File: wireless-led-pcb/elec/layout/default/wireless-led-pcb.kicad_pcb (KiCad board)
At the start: 2 copper layers, 40 x 40 mm, 37 parts

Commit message: Layout "done" but tbh it's super unverified.
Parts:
- added REF**: MountingHole_3.2mm_M3, MountingHole:MountingHole_3.2mm_M3, F.Cu at (49.0, 96.0)
- added REF**: MountingHole_3.2mm_M3, MountingHole:MountingHole_3.2mm_M3, F.Cu at (160.0, 85.0)
- added REF**: MountingHole_3.2mm_M3, MountingHole:MountingHole_3.2mm_M3, F.Cu at (180.0, 85.0)
- R4: value 100mW Thick Film Resistors 75V ±100ppm/℃ ±1% 732kΩ 0603 Chip Resistor - Surface Mount ROHS -> 100mW Thick Film Resistors 150V ±100ppm/℃ ±1% 732kΩ 0603 Chip Resistor - Surface Mount ROHS
- U10, U7, U8, U9: footprint TerminalBlock_Phoenix:TerminalBlock_Phoenix_MKDS-1,5-2_1x02_P5.00mm_Horizontal -> TerminalBlock_Phoenix:TerminalBlock_Phoenix_MKDS-1,5-3_1x03_P5.00mm_Horizontal
- moved U11 148.8 mm to (45.6, 79.4)
- moved U6 123.2 mm to (44.0, 91.0), turned to -90 degrees
- moved U8 74.0 mm to (171.0, 95.0), turned to 0 degrees
- moved U7 70.7 mm to (154.0, 95.0), turned to 0 degrees
- moved R2 62.8 mm to (115.5, 79.0), turned to 180 degrees
- moved U1 62.5 mm to (118.0, 75.0), turned to 180 degrees
- moved R1 56.4 mm to (120.5, 79.0)
- moved U9 55.1 mm to (181.0, 75.0), turned to 180 degrees
- moved Q1 51.5 mm to (90.5, 76.0), turned to 180 degrees
- moved R8 51.0 mm to (90.8, 79.0), turned to 180 degrees
- moved U4 46.4 mm to (107.2, 76.6), turned to 90 degrees
- moved C10 40.9 mm to (99.5, 73.0), turned to 180 degrees
- moved U15 40.5 mm to (125.3, 93.9), turned to -90 degrees
- moved U10 40.2 mm to (164.0, 75.0), turned to 180 degrees
- moved C7 38.5 mm to (83.5, 77.5), turned to 90 degrees
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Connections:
- C10 pad 1: ldo_5v-vcc -> level_shifter.ic-vcc
- Q1 pad 1: (no net) -> detect
- Q1 pad 2: (no net) -> boost_3v7_to_5v-vcc
- Q1 pad 3: (no net) -> led_strip_connector_1-vcc
- R8 pad 1: boost_3v7_to_5v-vcc -> detect
- U11 pad 1: (no net) -> led_strip_connector_1-vcc
- U11 pad 2: (no net) -> barrel_jack-vcc
- U11 pad 4: (no net) -> pole2_b
- U11 pad 5: (no net) -> battery_connector-vcc
- U14 pad 2: ldo_5v-vcc -> level_shifter.ic-vcc
- U4 pad 1: oe1 -> usb_connetor-gnd
- U4 pad 10: oe1 -> usb_connetor-gnd
- U4 pad 13: oe1 -> usb_connetor-gnd
- U4 pad 4: oe1 -> usb_connetor-gnd
- U4 pad 7: level_shifter.ic-gnd -> usb_connetor-gnd
- U5 pad 1: (no net) -> battery_connector-vcc
- U5 pad 2: (no net) -> usb_connetor-gnd
- U6 pad 1: (no net) -> barrel_jack-vcc
- U6 pad 2: (no net) -> usb_connetor-gnd
- U6 pad 3: (no net) -> detect
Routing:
- net led_strip_connector_1-vcc: track 0.00 -> 191.1 mm, vias 0 -> 3
- net battery_connector-vcc: track 0.00 -> 94.4 mm
- net mcu.ic-vcc-1: track 0.00 -> 90.6 mm, vias 0 -> 4
- net out2: track 0.00 -> 89.6 mm
- net out1: track 0.00 -> 74.2 mm
- net out3: track 0.00 -> 69.4 mm
- net usb_connetor-gnd: track 0.00 -> 61.6 mm, vias 0 -> 29
- net detect: track 0.00 -> 61.0 mm
- net boost_3v7_to_5v-vcc: track 0.00 -> 56.2 mm, vias 0 -> 2
- net out4: track 0.00 -> 55.2 mm
- net io14: track 0.00 -> 50.9 mm
- net pole2_b: track 0.00 -> 44.2 mm, vias 0 -> 1
- net io15: track 0.00 -> 42.8 mm
- net dp: track 0.00 -> 37.6 mm
- net dm: track 0.00 -> 37.0 mm
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- added copper zone on In1.Cu, net usb_connetor-gnd
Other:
- board size 40 x 40 mm -> 154 x 30 mm
- copper layers 2 -> 4

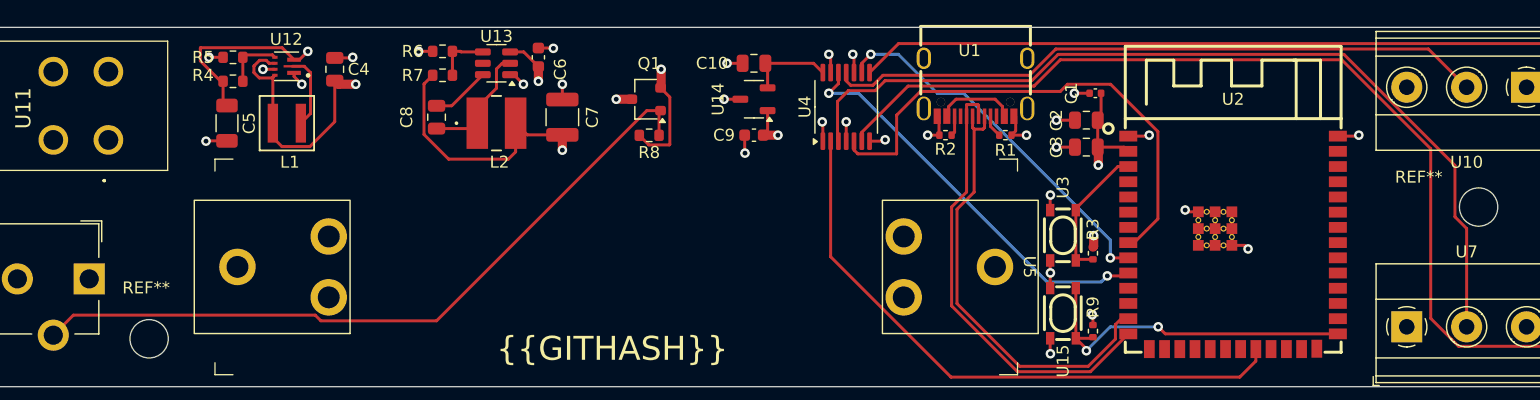
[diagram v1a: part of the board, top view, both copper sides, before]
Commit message: basic layout complete, smoke tested with jlcpcb.
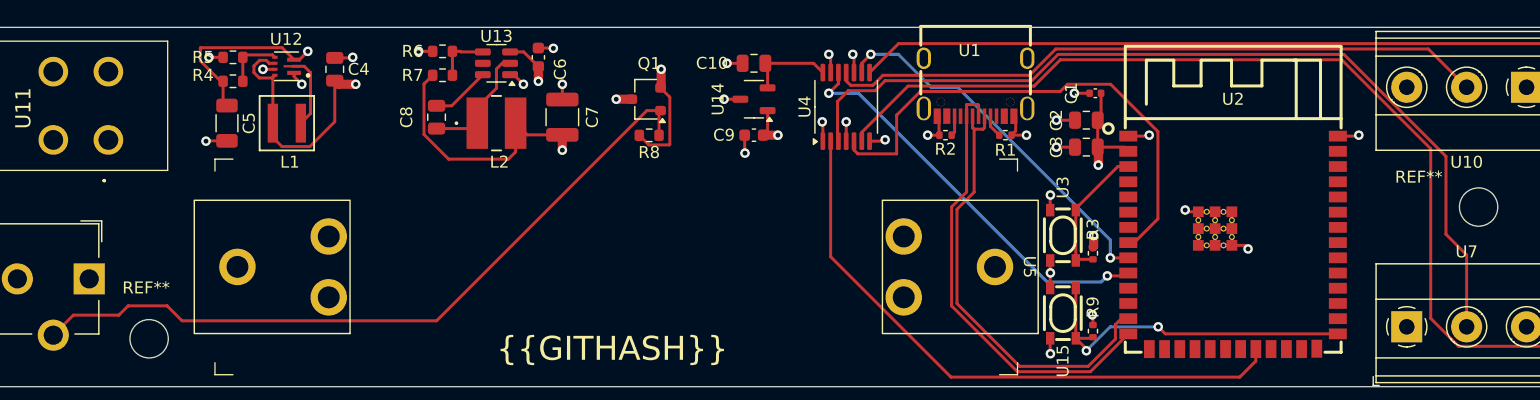
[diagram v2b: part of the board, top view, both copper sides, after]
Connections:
- U2 pad : (no net) -> usb_connetor-gnd
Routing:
- net usb_connetor-vcc: track 6.61 -> 0.00 mm
- net detect: track 61.0 -> 61.6 mm
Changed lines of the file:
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@@
 			(layers "*.Cu" "*.Paste" "*.Mask")
 			(remove_unused_layers no)
+			(net 8 "usb_connetor-gnd")
 		)
 		(pad "" thru_hole circle
@@
 			(layers "*.Cu" "*.Paste" "*.Mask")
 			(remove_unused_layers no)
+			(net 8 "usb_connetor-gnd")
 		)
 		(pad "" thru_hole circle
@@
 			(layers "*.Cu" "*.Paste" "*.Mask")
 			(remove_unused_layers no)
+			(net 8 "usb_connetor-gnd")
 		)
 		(pad "" thru_hole circle
@@
 			(layers "*.Cu" "*.Paste" "*.Mask")
 			(remove_unused_layers no)
+			(net 8 "usb_connetor-gnd")
 		)
 		(pad "" thru_hole circle
@@
 			(layers "*.Cu" "*.Paste" "*.Mask")
 			(remove_unused_layers no)
+			(net 8 "usb_connetor-gnd")
 		)
 		(pad "" thru_hole circle
@@
 			(layers "*.Cu" "*.Paste" "*.Mask")
 			(remove_unused_layers no)
+			(net 8 "usb_connetor-gnd")
 		)
 		(pad "" thru_hole circle
@@
 			(layers "*.Cu" "*.Paste" "*.Mask")
 			(remove_unused_layers no)
+			(net 8 "usb_connetor-gnd")
 		)
 		(pad "" thru_hole circle
@@
 			(layers "*.Cu" "*.Paste" "*.Mask")
 			(remove_unused_layers no)
+			(net 8 "usb_connetor-gnd")
 		)
 		(pad "" thru_hole circle
@@
 			(layers "*.Cu" "*.Paste" "*.Mask")
 			(remove_unused_layers no)
+			(net 8 "usb_connetor-gnd")
 		)
 		(pad "" thru_hole circle
@@
 			(layers "*.Cu" "*.Paste" "*.Mask")
 			(remove_unused_layers no)
+			(net 8 "usb_connetor-gnd")
 		)
 		(pad "" thru_hole circle
@@
 			(layers "*.Cu" "*.Paste" "*.Mask")
 			(remove_unused_layers no)
+			(net 8 "usb_connetor-gnd")
 		)
 		(pad "" thru_hole circle
@@
 			(layers "*.Cu" "*.Paste" "*.Mask")
 			(remove_unused_layers no)
+			(net 8 "usb_connetor-gnd")
 		)
 		(pad "1" smd rect
@@
 	)
 	(segment
-		(start 129.25 87.75)
-		(end 129.25 89.25)
+		(start 114.304695 75)
+		(end 116.5 75)
 		(width 0.25)
 		(layer "B.Cu")
@@
 	)
 	(segment
-		(start 114.809695 75.505)
-		(end 117.005 75.505)
+		(start 116.5 75)
+		(end 129.25 87.75)
 		(width 0.25)
 		(layer "B.Cu")
@@
 	)
 	(segment
-		(start 111.554695 72.25)
-		(end 114.809695 75.505)
+		(start 129.25 87.75)
+		(end 129.25 89.25)
 		(width 0.25)
 		(layer "B.Cu")
@@
 	)
 	(segment
-		(start 117.005 75.505)
-		(end 129.25 87.75)
+		(start 109.25 72.25)
+		(end 111.554695 72.25)
 		(width 0.25)
 		(layer "B.Cu")
@@
 	)
 	(segment
-		(start 109.25 72.25)
-		(end 111.554695 72.25)
+		(start 111.554695 72.25)
+		(end 114.304695 75)
 		(width 0.25)
 		(layer "B.Cu")
@@
 	)
 	(segment
-		(start 115.75 76.615305)
-		(end 115.75 77.41)
-		(width 0.25)
-		(layer "F.Cu")
-		(net 40)
-	)
-	(segment
-		(start 116.370305 75.995)
-		(end 115.75 76.615305)
-		(width 0.25)
-		(layer "F.Cu")
-		(net 40)
-	)
-	(segment
-		(start 120.25 77.42)
-		(end 120.25 76.615305)
-		(width 0.25)
-		(layer "F.Cu")
-		(net 40)
-	)
-	(segment
-		(start 120.25 76.615305)
-		(end 119.629695 75.995)
-		(width 0.25)
-		(layer "F.Cu")
-		(net 40)
-	)
-	(segment
-		(start 119.629695 75.995)
-		(end 116.370305 75.995)
-		(width 0.25)
-		(layer "F.Cu")
-		(net 40)
-	)
-	(segment
 		(start 116.25 78.75)
 		(end 116 79)
@@
 	)
 	(segment
-		(start 148.755 72.255)
-		(end 124.889544 72.255)
+		(start 107.384792 75.2875)
+		(end 107.380048 75.282757)
 		(width 0.25)
 		(layer "F.Cu")
@@
 	)
 	(segment
-		(start 124.889544 72.255)
-		(end 122.694544 74.45)
+		(start 159 89)
+		(end 157.274102 87.274102)
 		(width 0.25)
 		(layer "F.Cu")
@@
 	)
 	(segment
-		(start 107.380048 75.282757)
-		(end 106.475 76.187805)
+		(start 106.475 79.425)
+		(end 106.55 79.5)
 		(width 0.25)
 		(layer "F.Cu")
@@
 	)
 	(segment
-		(start 158.025 85.818072)
-		(end 158.025 81.525)
+		(start 157.274102 87.274102)
+		(end 157.274102 80.774102)
 		(width 0.25)
 		(layer "F.Cu")
@@
 	)
 	(segment
-		(start 110.452708 74.45)
-		(end 109.615208 75.2875)
+		(start 124.889544 72.255)
+		(end 122.694544 74.45)
 		(width 0.25)
 		(layer "F.Cu")
@@
 	)
 	(segment
-		(start 107.384792 75.2875)
-		(end 107.380048 75.282757)
+		(start 157.274102 80.774102)
+		(end 148.755 72.255)
 		(width 0.25)
 		(layer "F.Cu")
@@
 	)
 	(segment
-		(start 122.694544 74.45)
-		(end 110.452708 74.45)
+		(start 109.615208 75.2875)
+		(end 107.384792 75.2875)
 		(width 0.25)
 		(layer "F.Cu")
@@
 	)
 	(segment
-		(start 158.025 81.525)
-		(end 148.755 72.255)
+		(start 106.475 76.187805)
+		(end 106.475 79.425)
 		(width 0.25)
 		(layer "F.Cu")
@@
 	)
 	(segment
-		(start 159 86.793072)
-		(end 158.025 85.818072)
+		(start 107.380048 75.282757)
+		(end 106.475 76.187805)
 		(width 0.25)
 		(layer "F.Cu")
@@
 	)
 	(segment
-		(start 109.615208 75.2875)
-		(end 107.384792 75.2875)
+		(start 122.694544 74.45)
+		(end 110.452708 74.45)
 		(width 0.25)
 		(layer "F.Cu")
@@
 	(segment
 		(start 159 95)
-		(end 159 86.793072)
+		(end 159 89)
 		(width 0.25)
 		(layer "F.Cu")
@@
 	)
 	(segment
-		(start 106.475 79.425)
-		(end 106.55 79.5)
+		(start 110.452708 74.45)
+		(end 109.615208 75.2875)
 		(width 0.25)
 		(layer "F.Cu")
@@
 	)
 	(segment
-		(start 106.475 76.187805)
-		(end 106.475 79.425)
+		(start 148.755 72.255)
+		(end 124.889544 72.255)
 		(width 0.25)
 		(layer "F.Cu")
@@
 	)
 	(segment
+		(start 41 95.7)
+		(end 42.675 94.025)
+		(width 0.25)
+		(layer "F.Cu")
+		(net 61)
+	)
+	(segment
 		(start 73 94.5)
 		(end 90.55 76.95)
@@
 	)
 	(segment
-		(start 62.867119 94.025)
-		(end 63.342119 94.5)
+		(start 42.675 94.025)
+		(end 46.475 94.025)
 		(width 0.25)
 		(layer "F.Cu")
@@
 	)
 	(segment
-		(start 41 95.7)
-		(end 42.675 94.025)
+		(start 50.5 93.25)
+		(end 51.75 94.5)
 		(width 0.25)
 		(layer "F.Cu")
@@
 	)
 	(segment
-		(start 90.55 76.95)
-		(end 91.7 76.95)
+		(start 46.475 94.025)
+		(end 47.25 93.25)
 		(width 0.25)
 		(layer "F.Cu")
@@
 	)
 	(segment
-		(start 42.675 94.025)
-		(end 62.867119 94.025)
+		(start 90.55 76.95)
+		(end 91.7 76.95)
 		(width 0.25)
 		(layer "F.Cu")
@@
 	)
 	(segment
-		(start 63.342119 94.5)
-		(end 73 94.5)
+		(start 47.25 93.25)
+		(end 50.5 93.25)
 		(width 0.25)
 		(layer "F.Cu")
@@
 		(width 0.25)
 		(layer "F.Cu")
+		(net 61)
+	)
+	(segment
+		(start 51.75 94.5)
+		(end 73 94.5)
+		(width 0.25)
+		(layer "F.Cu")

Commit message: added test points
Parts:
- added J1: , TestPoint:TestPoint_Keystone_5005-5009_Compact, F.Cu at (170.5, 87.0)
- added J2: , TestPoint:TestPoint_Keystone_5005-5009_Compact, F.Cu at (50.5, 86.5)
- added J3: , TestPoint:TestPoint_Keystone_5005-5009_Compact, F.Cu at (174.5, 83.0)
- added J4: , TestPoint:TestPoint_Keystone_5005-5009_Compact, F.Cu at (166.5, 83.0)
- added J5: , TestPoint:TestPoint_Keystone_5005-5009_Compact, F.Cu at (166.5, 87.0)
- added J6: , TestPoint:TestPoint_Keystone_5005-5009_Compact, F.Cu at (50.5, 90.5)
- added J7: , TestPoint:TestPoint_Keystone_5005-5009_Compact, F.Cu at (170.5, 83.0)
- added J8: , TestPoint:TestPoint_Keystone_5005-5009_Compact, F.Cu at (174.5, 87.0)
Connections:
- net io14 renamed tp
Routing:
- net boost_3v7_to_5v-vcc: track 56.2 -> 165.9 mm
- net level_shifter.ic-vcc: track 7.25 -> 81.5 mm, vias 0 -> 4
- net tp: track 50.9 -> 105.3 mm
- net mcu.ic-vcc-1: track 90.6 -> 136.6 mm, vias 4 -> 7
- net battery_connector-vcc: track 94.4 -> 111.7 mm
- net led_strip_connector_1-vcc: track 191.1 -> 200.2 mm
- net detect: track 61.6 -> 64.4 mm

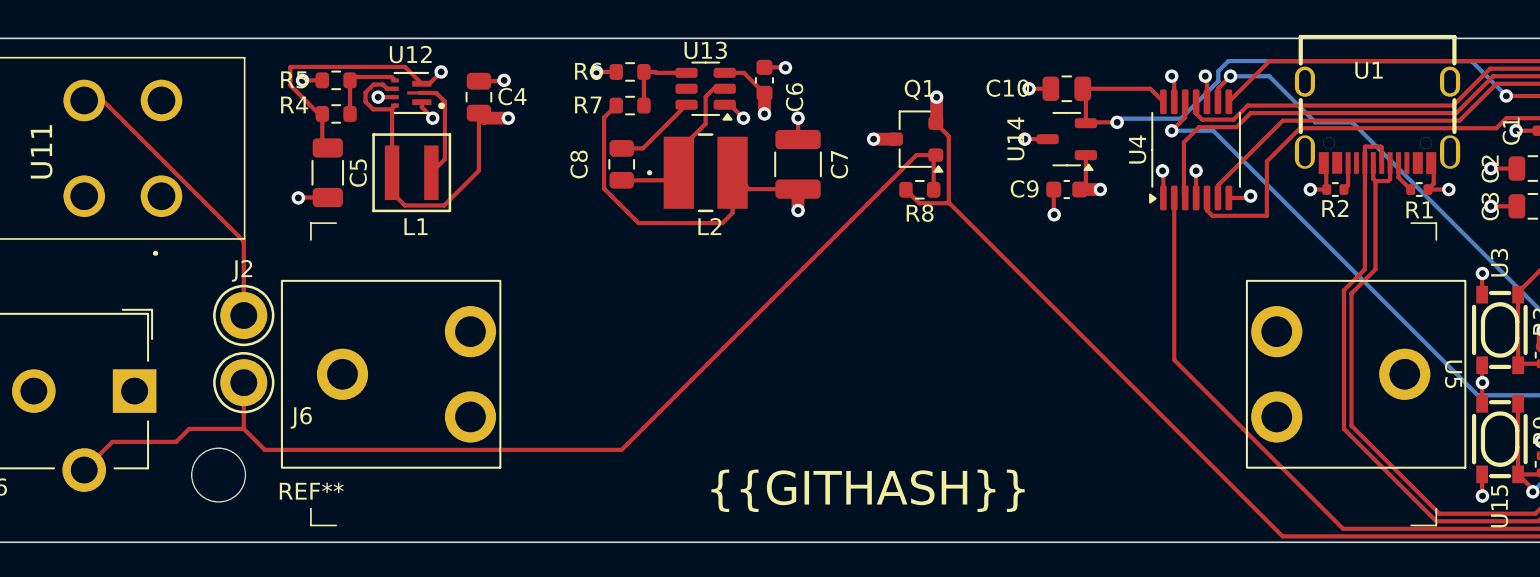
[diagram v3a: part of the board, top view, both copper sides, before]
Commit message: fixed battery holder footprint to fit longer cell
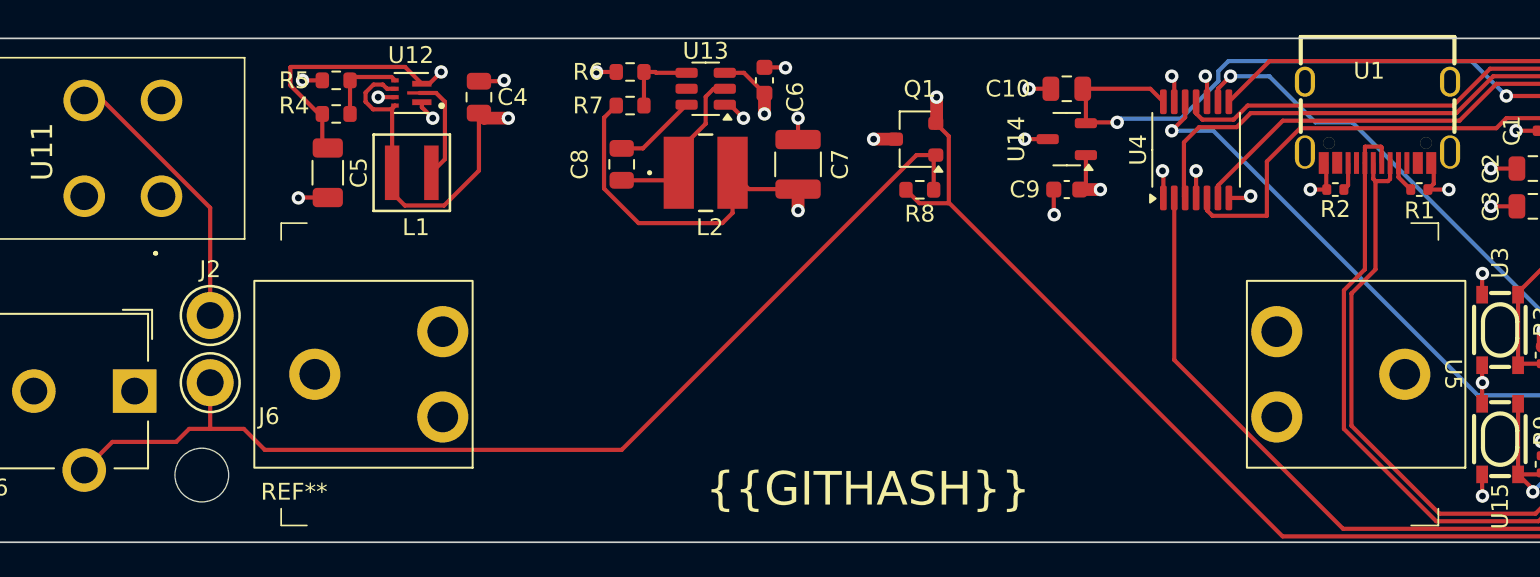
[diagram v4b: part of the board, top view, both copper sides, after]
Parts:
- moved J2 2.00 mm to (48.5, 86.5)
- moved J6 2.00 mm to (48.5, 90.5)
- moved REF** 1.00 mm to (48.0, 96.0)
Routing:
- net battery_connector-vcc: track 111.7 -> 110.9 mm
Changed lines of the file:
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@@
 	(footprint "TestPoint:TestPoint_Keystone_5005-5009_Compact"
 		(layer "F.Cu")
-		(at 50.5 90.5)
+		(at 48.5 90.5)
 		(descr "Keystone Miniature THM Test Point 5005-5009, http://www.keyelco.com/product-pdf.cfm?p=1314")
 		(tags "Through Hole Mount Test Points")
@@
 	(footprint "MountingHole:MountingHole_3.2mm_M3"
 		(layer "F.Cu")
-		(at 49 96)
+		(at 48 96)
 		(descr "Mounting Hole 3.2mm, no annular, M3")
 		(tags "mounting hole 3.2mm no annular m3")
@@
 			)
 		)
-		(property "Footprint" ""
+		(property "Footprint" "lib:Battery-54"
 			(at 0 0 90)
 			(layer "F.Fab")
@@
 		(attr through_hole)
 		(fp_line
-			(start -9 57.5056)
-			(end -9 56)
+			(start -8 59.278)
+			(end -9 59.278)
 			(stroke
 				(width 0.1)
@@
 		)
 		(fp_line
-			(start -8 57.5056)
-			(end -9 57.5056)
+			(start 9 59.278)
+			(end 8 59.278)
 			(stroke
 				(width 0.1)
@@
 		)
 		(fp_line
-			(start 9 57.5056)
-			(end 8 57.5056)
+			(start -9 59.2528)
+			(end -9 57.7472)
 			(stroke
 				(width 0.1)
@@
 		)
 		(fp_line
-			(start 9 56)
-			(end 9 57.5056)
+			(start 9 57.7472)
+			(end 9 59.2528)
 			(stroke
 				(width 0.1)
@@
 		(fp_line
 			(start -9 -8)
-			(end -9 -9.4996)
+			(end -9 -9.622)
 			(stroke
 				(width 0.1)
@@
 		)
 		(fp_line
-			(start -9 -9.4996)
-			(end -8 -9.4996)
+			(start -9 -9.622)
+			(end -8 -9.622)
 			(stroke
 				(width 0.1)
@@
 		)
 		(fp_line
-			(start 8 -9.4996)
-			(end 9 -9.4996)
+			(start 8 -9.622)
+			(end 9 -9.622)
 			(stroke
 				(width 0.1)
@@
 		)
 		(fp_line
-			(start 9 -9.4996)
+			(start 9 -9.622)
 			(end 9 -8)
 			(stroke
@@
 		)
 		(fp_rect
-			(start 5.5626 46.228)
-			(end -5.5626 59.2328)
+			(start 5.5626 47.878)
+			(end -5.5626 60.878)
 			(stroke
 				(width 0.12)
@@
 		)
 		(pad "2" thru_hole circle
-			(at -2.54 48.006 270)
+			(at -2.54 49.656 270)
 			(size 3.048 3.048)
 			(drill 1.8288)
@@
 		)
 		(pad "2" thru_hole circle
-			(at 0 55.626 270)
+			(at 0 57.276 270)
 			(size 3.048 3.048)
 			(drill 1.8288)
@@
 		)
 		(pad "2" thru_hole circle
-			(at 2.54 48.006 270)
+			(at 2.54 49.656 270)
 			(size 3.048 3.048)
 			(drill 1.8288)
@@
 	(footprint "TestPoint:TestPoint_Keystone_5005-5009_Compact"
 		(layer "F.Cu")
-		(at 50.5 86.5)
+		(at 48.5 86.5)
 		(descr "Keystone Miniature THM Test Point 5005-5009, http://www.keyelco.com/product-pdf.cfm?p=1314")
 		(tags "Through Hole Mount Test Points")
@@
 	)
 	(segment
-		(start 50.5 82.087791)
-		(end 42.109709 73.6975)
+		(start 42.109709 73.6975)
+		(end 41 73.6975)
 		(width 0.25)
 		(layer "F.Cu")
@@
 	)
 	(segment
-		(start 42.109709 73.6975)
-		(end 41 73.6975)
+		(start 48.5 86.5)
+		(end 48.5 80.087791)
 		(width 0.25)
 		(layer "F.Cu")
@@
 	)
 	(segment
-		(start 50.5 86.5)
-		(end 50.5 82.087791)
+		(start 48.5 80.087791)
+		(end 42.109709 73.6975)
 		(width 0.25)
 		(layer "F.Cu")
@@
 	)
 	(segment
-		(start 63.12508 89.565)
-		(end 54.81008 81.25)
-		(width 0.762)
-		(layer "In2.Cu")
-		(net 60)
-	)
-	(segment
-		(start 54.81008 81.25)
+		(start 60.75 81.25)
 		(end 44.880752 81.25)
 		(width 0.762)
@@
 	)
 	(segment
-		(start 112.003 87.46)
-		(end 109.898 89.565)
+		(start 44.880752 81.25)
+		(end 43 79.369248)
 		(width 0.762)
 		(layer "In2.Cu")
@@
 	)
 	(segment
+		(start 112.003 87.46)
+		(end 109.898 89.565)
+		(width 0.762)
+		(layer "In2.Cu")
+		(net 60)
+	)
+	(segment
 		(start 43 79.369248)
 		(end 43 75.6975)
@@
 	)
 	(segment
-		(start 109.898 89.565)
-		(end 63.12508 89.565)
+		(start 69.065 89.565)
+		(end 60.75 81.25)
 		(width 0.762)
 		(layer "In2.Cu")
@@
 	)
 	(segment
-		(start 44.880752 81.25)
-		(end 43 79.369248)
+		(start 109.898 89.565)
+		(end 69.065 89.565)
 		(width 0.762)
 		(layer "In2.Cu")
@@
 	)
 	(segment
-		(start 50.5 90.5)
-		(end 50.5 93.25)
-		(width 0.25)
-		(layer "F.Cu")
-		(net 61)
-	)
-	(segment
 		(start 73 94.5)
 		(end 90.55 76.95)
@@
 	)
 	(segment
+		(start 47.25 93.25)
+		(end 48.5 93.25)
+		(width 0.25)
+		(layer "F.Cu")
+		(net 61)
+	)
+	(segment
 		(start 91.575 77.075)
 		(end 91.7 76.95)
@@
 	)
 	(segment
-		(start 47.25 93.25)
+		(start 48.5 90.5)
+		(end 48.5 93.25)
+		(width 0.25)
+		(layer "F.Cu")
+		(net 61)
+	)
+	(segment
+		(start 48.5 93.25)
 		(end 50.5 93.25)
 		(width 0.25)
